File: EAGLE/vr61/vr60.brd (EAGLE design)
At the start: 283 x 93 mm, 227 parts, among them IC1 MC74VHC1G50, IC2 REG1117, J3 JTAG, J6 MICROMOD-2222-C

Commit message: pcb tracing done
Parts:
- J3: value JTAG -> (none); device SparkFun-Connectors:2X5-PTH-1.27MM -> SparkFun-Connectors:1X04
- moved J3 43.0 mm to (54.5, 76.0), flipped to the top
- moved D35 21.7 mm to (137.8, 40.5)
- moved D30 5.00 mm to (49.0, 44.1)
- moved D18 4.53 mm to (63.5, 63.4)
- moved D17 4.50 mm to (51.0, 63.4)
- moved JP1 3.00 mm to (30.0, 57.0), turned to 270 degrees
- moved D55 2.00 mm to (28.2, 17.9)
- moved D15 1.00 mm to (6.00, 63.0)
- moved D16 1.00 mm to (32.5, 63.4)
- moved R2 0.65 mm to (27.0, 89.7)
- moved C6 0.55 mm to (11.0, 89.5)
- moved J1 0.50 mm to (159.0, 9.50)
- moved X1 0.40 mm to (18.2, 95.9)
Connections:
- new net A0: J3.3, J6.34
- new net PWM: J3.2, J6.32
- net !RESET: no longer J3.10
- net GND: now also J3.1; no longer J3.3, J3.5, J3.9
- net SWDCK: no longer J3.4
- net SWDIO: no longer J3.2
- net VCC: now also J3.4; no longer J3.1
- net VSUP: now also J6.9
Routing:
- net MX1: track 166.5 -> 435.5 mm, vias 6 -> 11
- net MX6: track 138.0 -> 397.4 mm, vias 0 -> 6
- net !BOOT: track 0.00 -> 209.7 mm, vias 0 -> 4
- net MX5: track 159.5 -> 347.1 mm, vias 6 -> 10
- net MX4: track 173.2 -> 354.0 mm, vias 5 -> 7
- net MX2: track 204.9 -> 385.7 mm, vias 5 -> 7
- net MY3: track 4.10 -> 173.3 mm, vias 1 -> 2
- net MX0: track 180.2 -> 332.8 mm, vias 3 -> 8
- net MY8: track 98.0 -> 213.8 mm, vias 1 -> 3
- net MY6: track 120.5 -> 233.3 mm, vias 7 -> 8
- net N$29: track 0.00 -> 112.8 mm, vias 0 -> 4
- net MY5: track 95.7 -> 199.1 mm, vias 4 -> 3
- net MY7: track 109.6 -> 207.1 mm, vias 6 -> 3
- net MX7: track 216.0 -> 311.4 mm, vias 4 -> 8
- net VCC: track 31.0 -> 119.5 mm, vias 3 -> 5
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
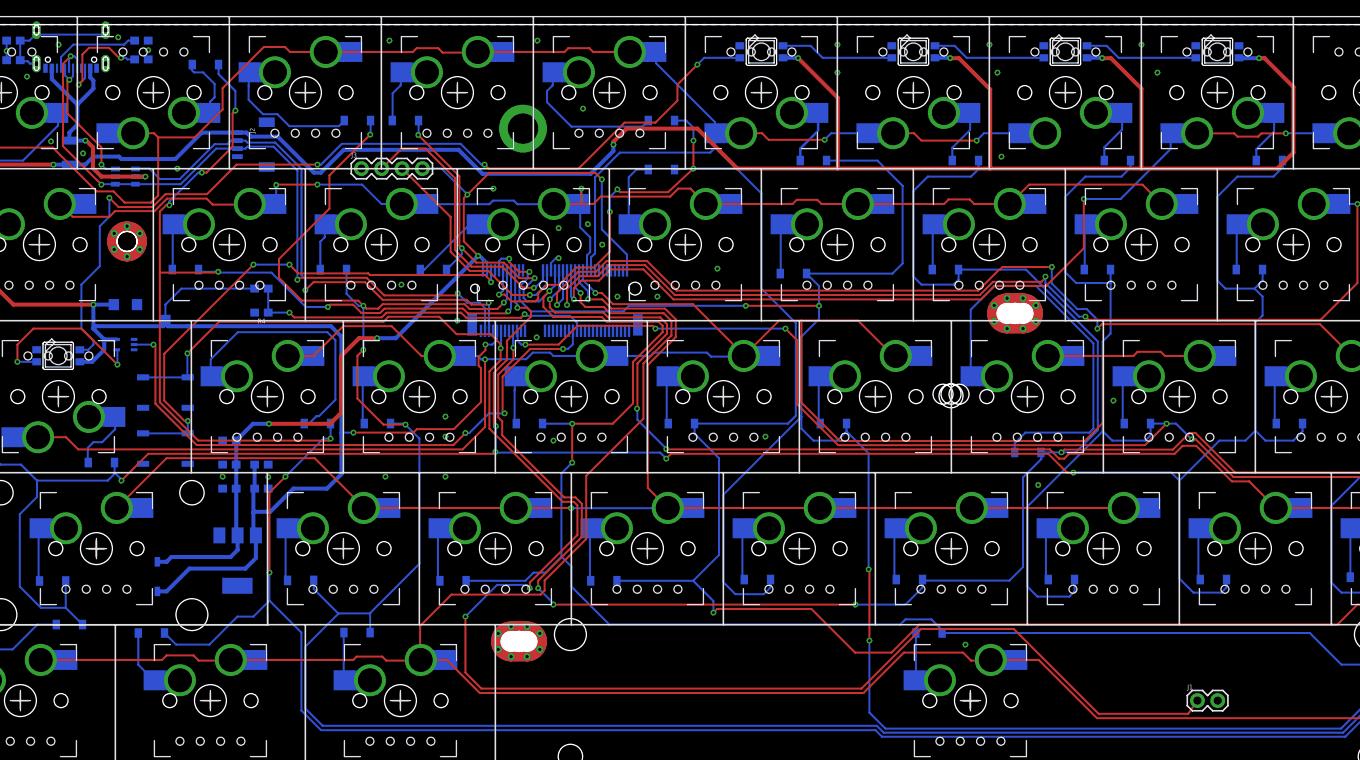
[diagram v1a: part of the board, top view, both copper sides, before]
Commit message: added heat sink on 1117
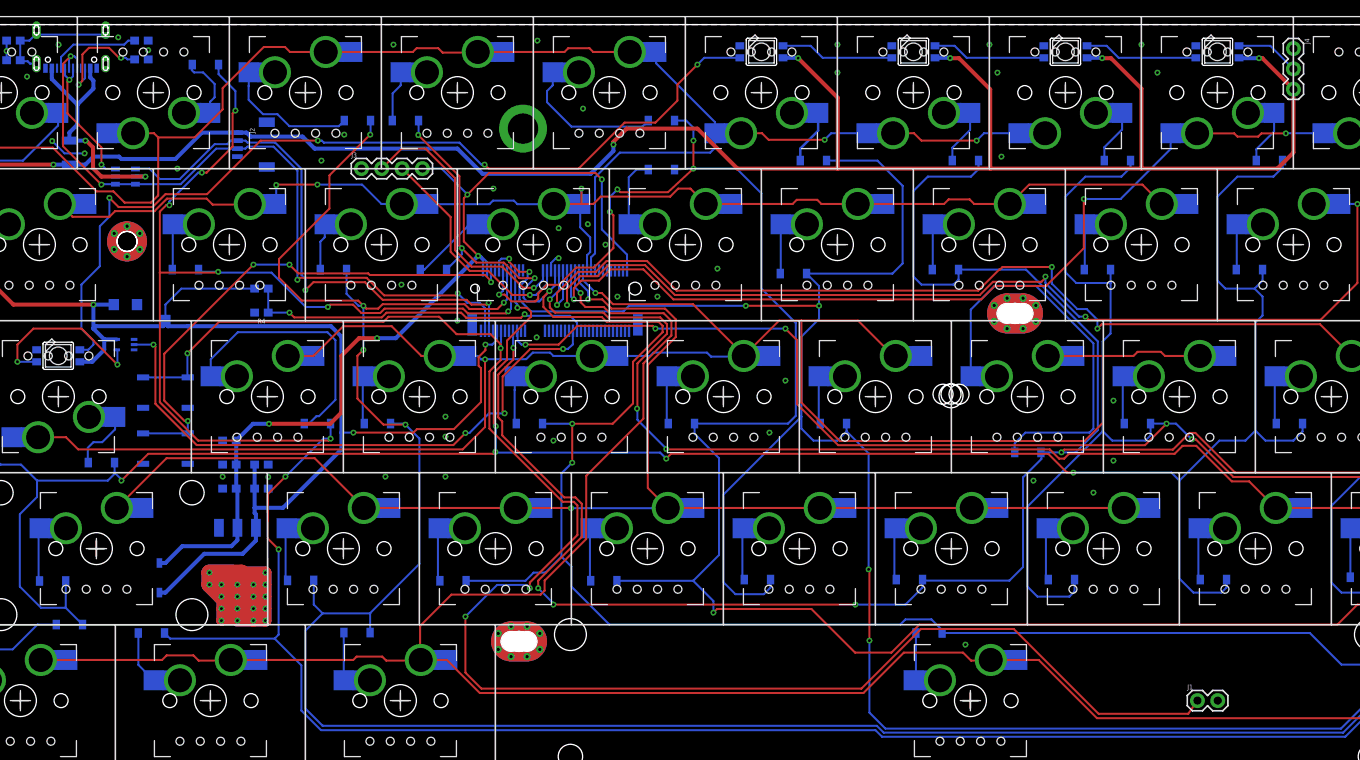
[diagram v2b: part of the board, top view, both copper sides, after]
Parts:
- removed IC2: REG1117, burr-brown:SOT223
- added J4: (no value), SparkFun-Connectors:1X03
- added U1: (no value), SparkFun-IC-Power:SOT223
- moved D62 0.29 mm to (29.2, 24.9)
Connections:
- new net N$72: J4.2, LED-8.2-DOUT
- new net SINK: U1.4
- net GND: now also J4.1, U1.1; no longer IC2.1
- net VCC: now also U1.2; no longer IC2.2
- net VSUP: now also J4.3, U1.3; no longer IC2.3
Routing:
- net SINK: track 0.00 -> 106.0 mm, vias 0 -> 19
- net N$72: track 0.00 -> 8.00 mm
- net VSUP: track 407.9 -> 401.8 mm
- net GND: track 4.57 -> 9.27 mm, vias 41 -> 46
- net MX1: track 435.5 -> 434.1 mm
- net VCC: track 119.5 -> 118.5 mm

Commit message: wip, logos
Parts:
- removed SG3: MOUNTING-HOLE-WIDE, ts_keyboards:MOUNTING-HOLE-WIDE
- added LOGO1: OSHW-LOGOL, random_logos:OSHW-LOGO-L
- added U$5: SPARKFUN_LOGO0.2, random_logos:SFE_LOGO_NAME_FLAME_.2
- SG1, SG4: value MOUNTING-HOLE-VWIDE -> MOUNTING-HOLE-VWIDEEDGE-CUT; device ts_keyboards:MOUNTING-HOLE-VWIDE -> ts_keyboards:MOUNTING-HOLE-VWIDE-C
- moved D58 14.5 mm to (196.3, 17.5)
- moved IC1 14.1 mm to (23.0, 40.0)
- moved LED-CL 10.2 mm to (16.6, 42.4)
- moved D29 6.32 mm to (16.0, 37.2)
- moved U$14 1.00 mm to (24.0, 59.0), turned to 0 degrees
- turned SG4 to 180 degrees
- turned S_CPS to 0 degrees
- turned S_FN1 to 0 degrees
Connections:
- removed net SG3: SG3.P$10, SG3.P$2, SG3.P$3, SG3.P$4, SG3.P$5, SG3.P$7, SG3.P$8, SG3.P$9
- net SG1: no longer SG1.P$10, SG1.P$2, SG1.P$3, SG1.P$9
- net SG4: no longer SG4.P$10, SG4.P$2, SG4.P$3, SG4.P$9
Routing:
- net N$29: track 113.1 -> 128.1 mm
- net VSUP: track 401.8 -> 413.1 mm
- net N$70: track 21.6 -> 12.4 mm, vias 2 -> 0
- net N$62: track 7.79 -> 15.7 mm
- net N$58: track 11.1 -> 5.51 mm
- net LED: track 74.2 -> 72.0 mm
- net MY4: track 355.0 -> 352.9 mm
- net MY2: track 247.6 -> 249.5 mm, vias 2 -> 3
- net MX0: track 332.8 -> 332.1 mm
- net MX5: track 347.1 -> 346.7 mm, vias 10 -> 9
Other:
- board text added: "(c) Vino Rodrigues"
- board text added: "MicroMod"
- board text added: "tecsmith.com.au"
- board text removed: "JTAG"

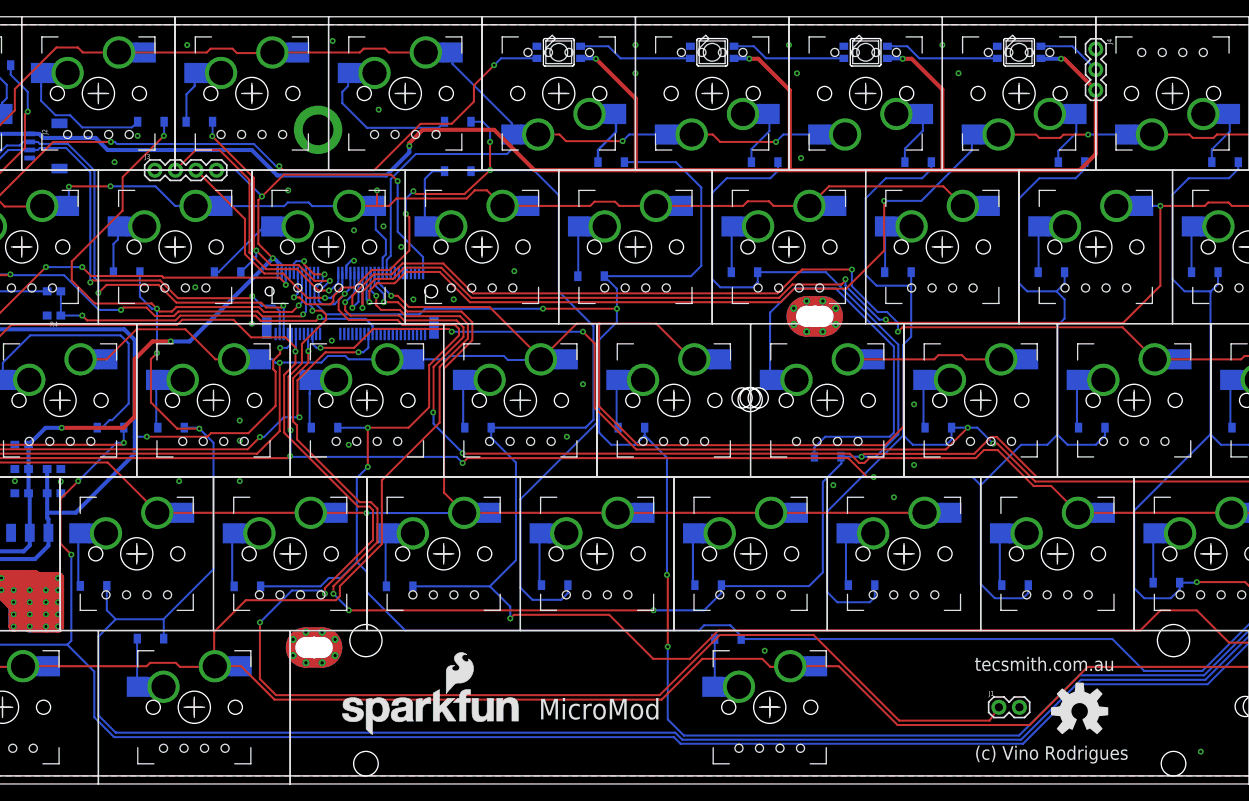
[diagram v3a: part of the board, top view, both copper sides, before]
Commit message: logos and text
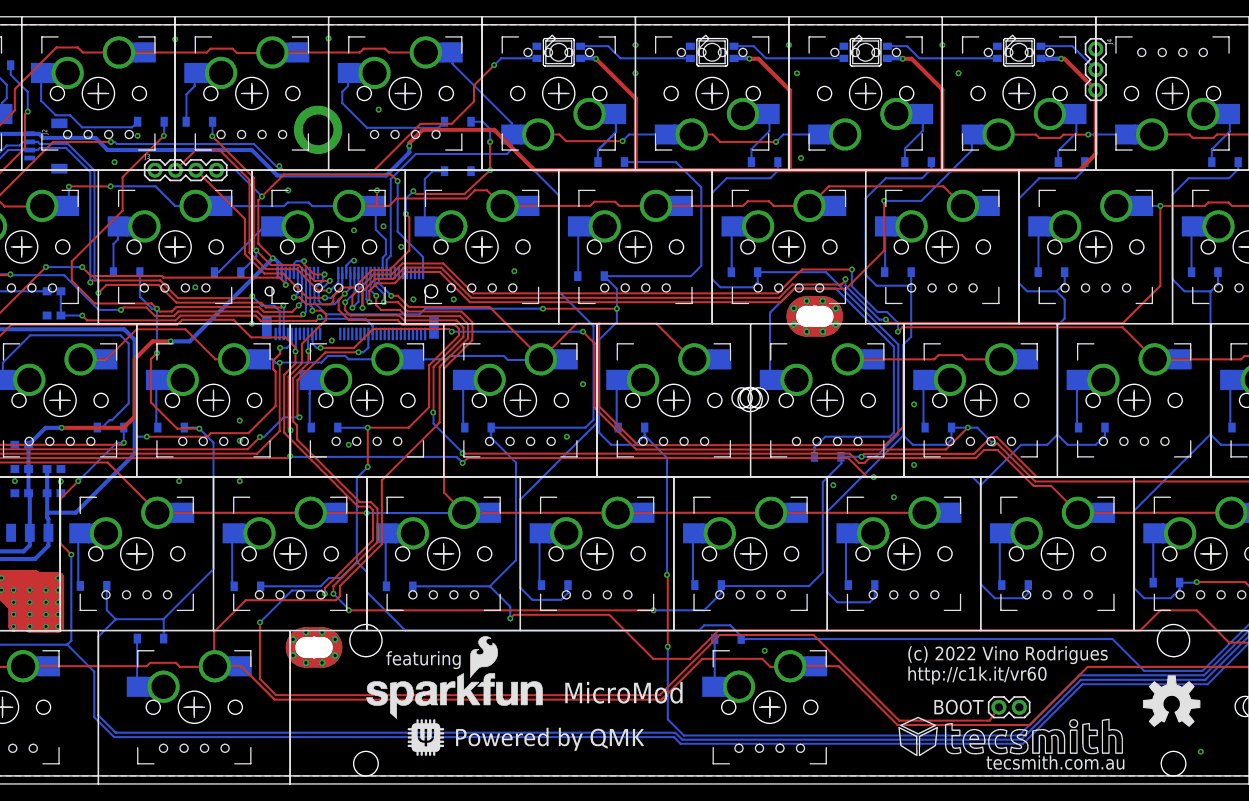
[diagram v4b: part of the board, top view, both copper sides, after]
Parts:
- added LOGO2: OSHW-LOGOL, random_logos:OSHW-LOGO-L
- added PTC: PTC_ASMD1206, ts_keyboards:SMD_PTC
- added U$10: SPARKFUN_LOGO0.2, random_logos:SFE_LOGO_NAME_FLAME_.2
- added U$12, U$6: QMK_LOGO, random_logos:QMK_LOGO
- added U$8: TECSMITH-LOGOLONG, random_logos:TECSMITH-NAME
- U$7: value PTC_ASMD1206 -> TECSMITH-LOGOLONG; device ts_keyboards:SMD_PTC -> random_logos:TECSMITH-NAME
- moved U$7 170.0 mm to (172.0, 6.00), turned to 0 degrees
- moved LOGO1 11.4 mm to (180.4, 9.90)
- moved U$5 3.61 mm to (80.0, 8.00)
- renumbered IC1 to L/SFT, U$14 to TVS, U$3 to ESD
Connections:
- net VBUS: now also PTC.P$1; no longer U$7.P$1
- net VSUP: now also PTC.P$2; no longer U$7.P$2
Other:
- board text added: "(c) 2022 Vino Rodrigues http://c1k.it/vr60"
- board text added: "3V3"
- board text added: "A0"
- board text added: "ESD"
- board text added: "GND"
- board text added: "JLCJLCJLCJLC"
- board text added: "LED@5"
- board text added: "PTC"
- board text added: "PWM"
- board text added: "V/REG"
- board text added: "V5"
- board text added: "VIN/3"
- board text added: "Ver 1.0 | Rev 2022-06-06"
- board text added: "featuring"
- board text removed: "(c) Vino Rodrigues"
